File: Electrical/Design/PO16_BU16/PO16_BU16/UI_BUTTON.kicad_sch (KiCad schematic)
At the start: 32 parts

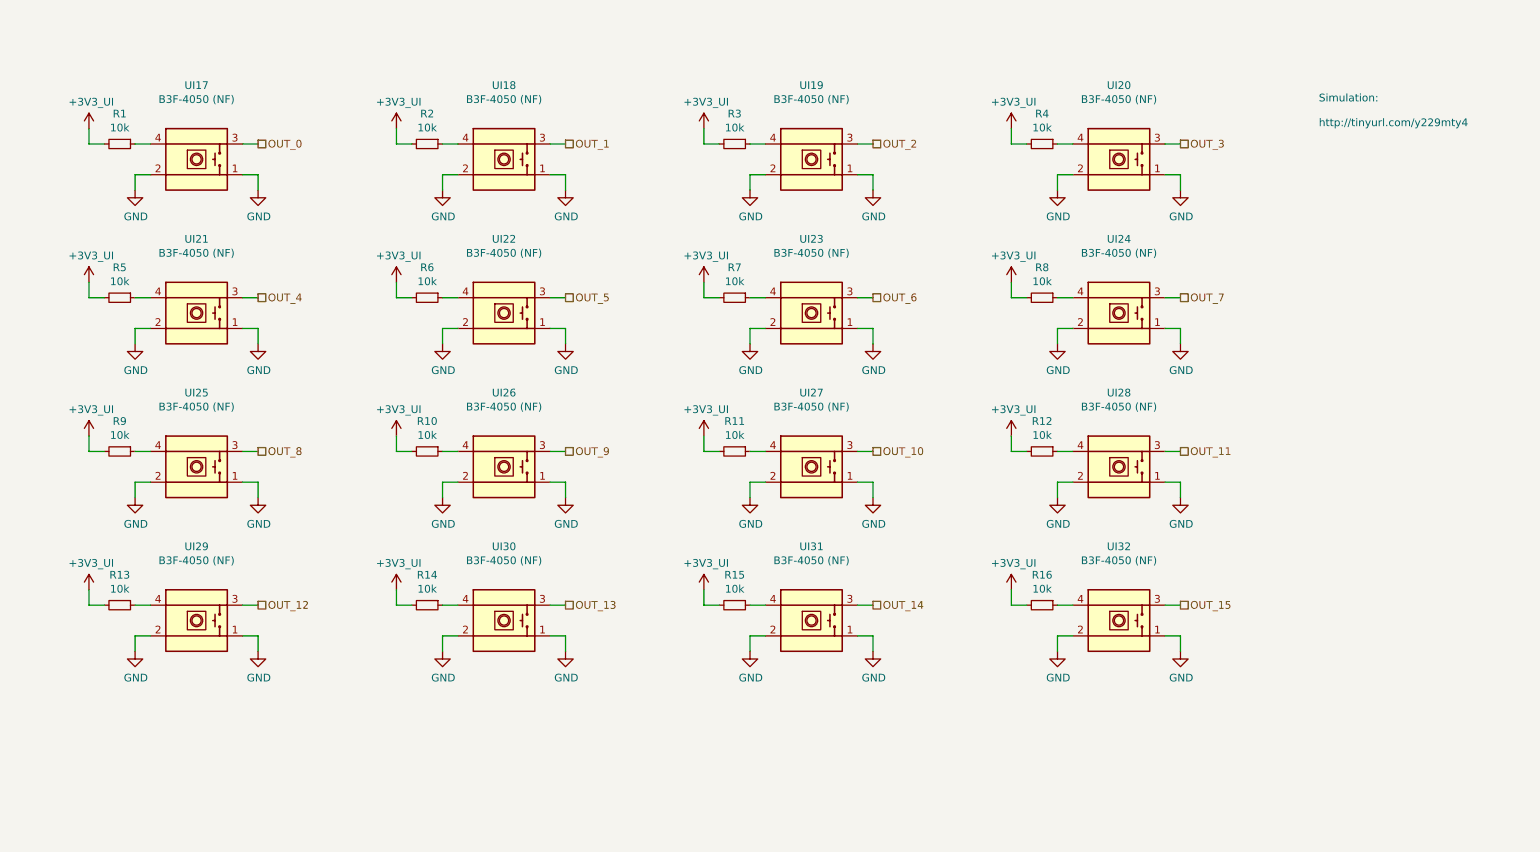
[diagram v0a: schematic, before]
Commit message: SUKU po16_bu16 cloned from pbf4
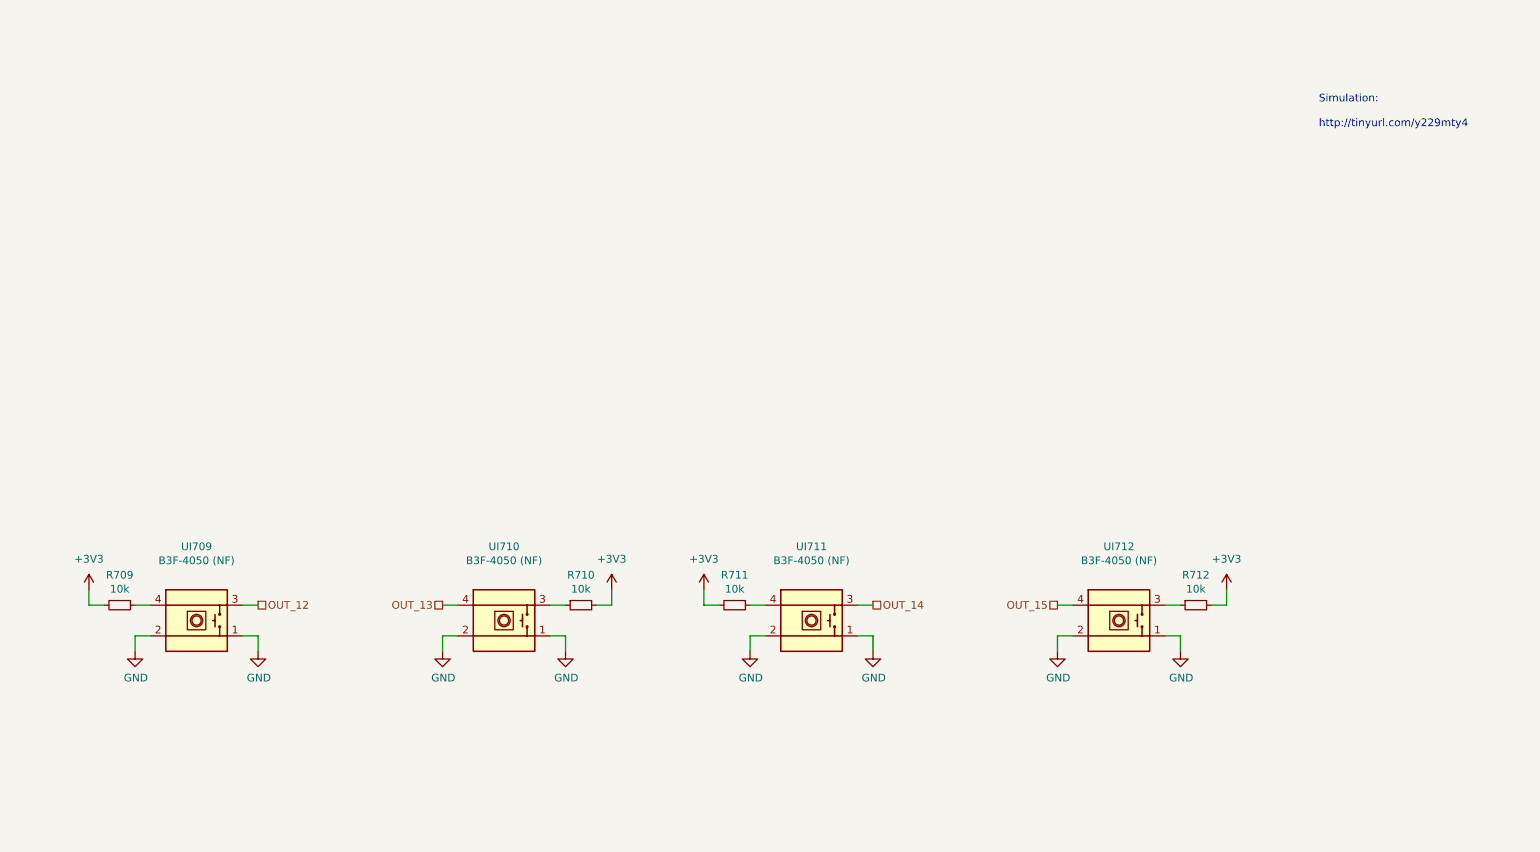
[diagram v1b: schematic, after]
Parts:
- removed R1, R10, R11, R12, R2, R3, R4, R5, R6, R7, R8, R9: 10k, suku_basics:RES_0805, symbol suku_basics:RES
- removed UI17, UI18, UI19, UI20, UI21, UI22, UI23, UI24, UI25, UI26, UI27, UI28: B3F-4050 (NF), suku_basics:UI_BUTTON_OMRON, symbol suku_basics:UI_Pushbutton_Omron
- R709: renamed from R13; footprint suku_basics:RES_0805 -> suku_basics:RES_0402
- R710: renamed from R14; footprint suku_basics:RES_0805 -> suku_basics:RES_0402
- R711: renamed from R15; footprint suku_basics:RES_0805 -> suku_basics:RES_0402
- R712: renamed from R16; footprint suku_basics:RES_0805 -> suku_basics:RES_0402
- renumbered UI29 to UI709, UI30 to UI710, UI31 to UI711, UI32 to UI712
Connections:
- net OUT_13: now also UI710.4; no longer UI710.3
- net OUT_15: now also UI712.4; no longer UI712.3
- net at R710.1: now also UI710.3; no longer UI710.4
- net at R712.1: now also UI712.3; no longer UI712.4
- net +3V3_UI renamed +3V3
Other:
- moved on the sheet: R710, R712

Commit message: SUKU PO16_BU16 updated design routed
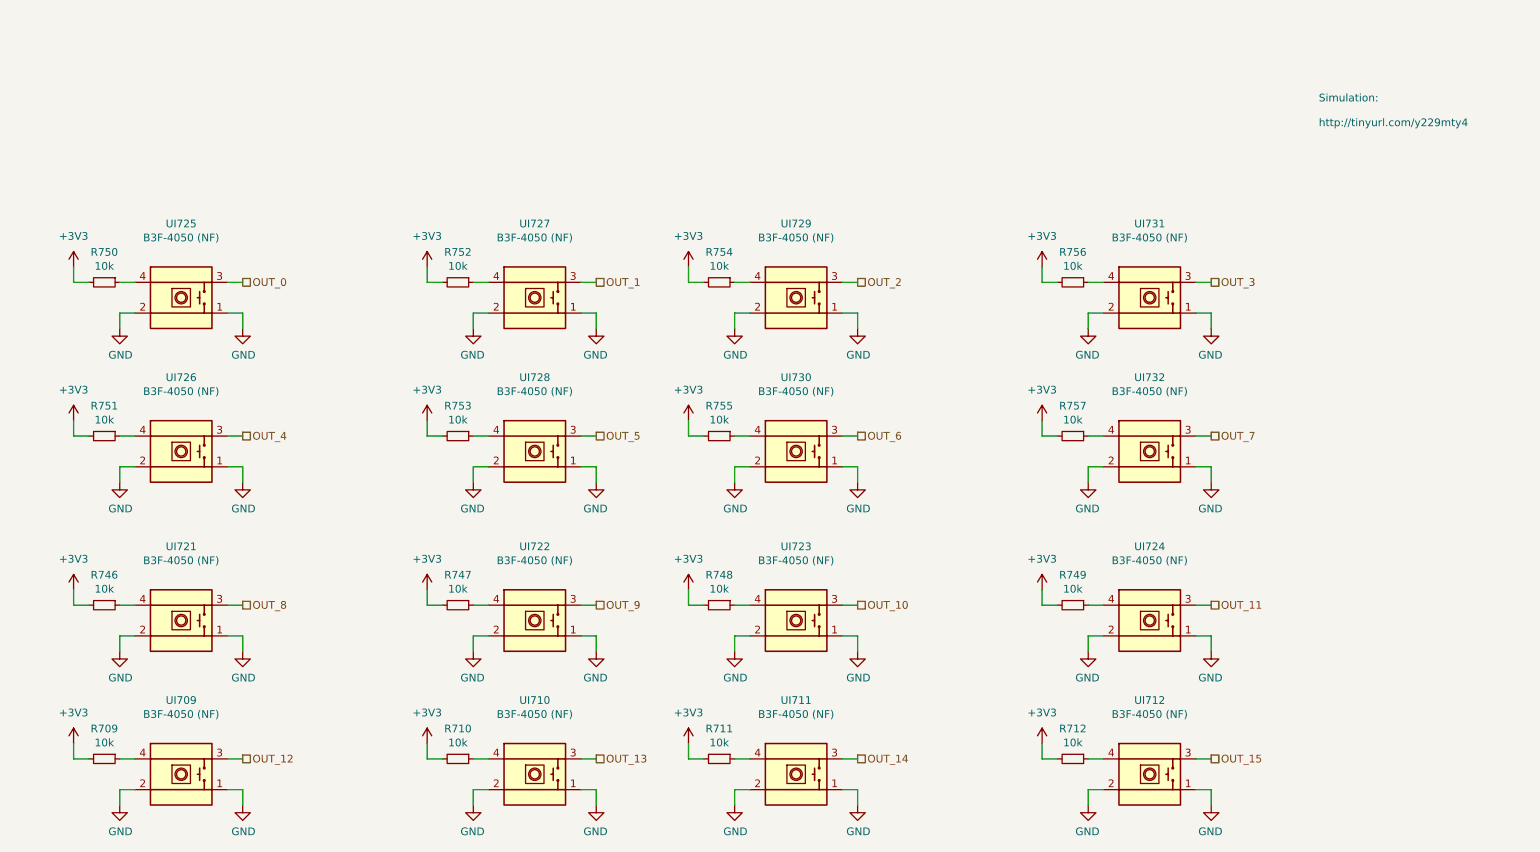
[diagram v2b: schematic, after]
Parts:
- added R746, R747, R748, R749, R750, R751, R752, R753, R754, R755, R756, R757: 10k, suku_basics:RES_0402, symbol suku_basics:RES
- added UI721, UI722, UI723, UI724, UI725, UI726, UI727, UI728, UI729, UI730, UI731, UI732: B3F-4050 (NF), suku_basics:UI_BUTTON_OMRON, symbol suku_basics:UI_Pushbutton_Omron
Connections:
- net +3V3: now also R746.2, R747.2, R748.2, R749.2, R750.2, R751.2, R752.2, R753.2, R754.2, R755.2, R756.2, R757.2
- net GND: now also UI721.1, UI721.2, UI722.1, UI722.2, UI723.1, UI723.2, UI724.1, UI724.2, UI725.1, UI725.2, UI726.1, UI726.2, UI727.1, UI727.2, UI728.1, UI728.2, UI729.1, UI729.2, UI730.1, UI730.2, UI731.1, UI731.2, UI732.1, UI732.2
- net OUT_13: now also UI710.3; no longer UI710.4
- net OUT_15: now also UI712.3; no longer UI712.4
- net at R710.1: now also UI710.4; no longer UI710.3
- net at R712.1: now also UI712.4; no longer UI712.3
- new net: R754.1, UI729.4
- new net: R753.1, UI728.4
- new net: R748.1, UI723.4
- new net: R747.1, UI722.4
- new net: R752.1, UI727.4
- new net: R746.1, UI721.4
- new net: R757.1, UI732.4
- new net: R756.1, UI731.4
- new net: R749.1, UI724.4
- new net: R750.1, UI725.4
- new net: R755.1, UI730.4
- new net: R751.1, UI726.4
- new net OUT_0: UI725.3
- new net OUT_1: UI727.3
- new net OUT_10: UI723.3
- new net OUT_11: UI724.3
- new net OUT_2: UI729.3
- new net OUT_3: UI731.3
- new net OUT_4: UI726.3
- new net OUT_5: UI728.3
- new net OUT_6: UI730.3
- new net OUT_7: UI732.3
- new net OUT_8: UI721.3
- new net OUT_9: UI722.3
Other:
- moved on the sheet: R709, R710, R711, R712, UI709, UI710, UI711, UI712

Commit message: SUKU PO16_BU16 sch reannotated
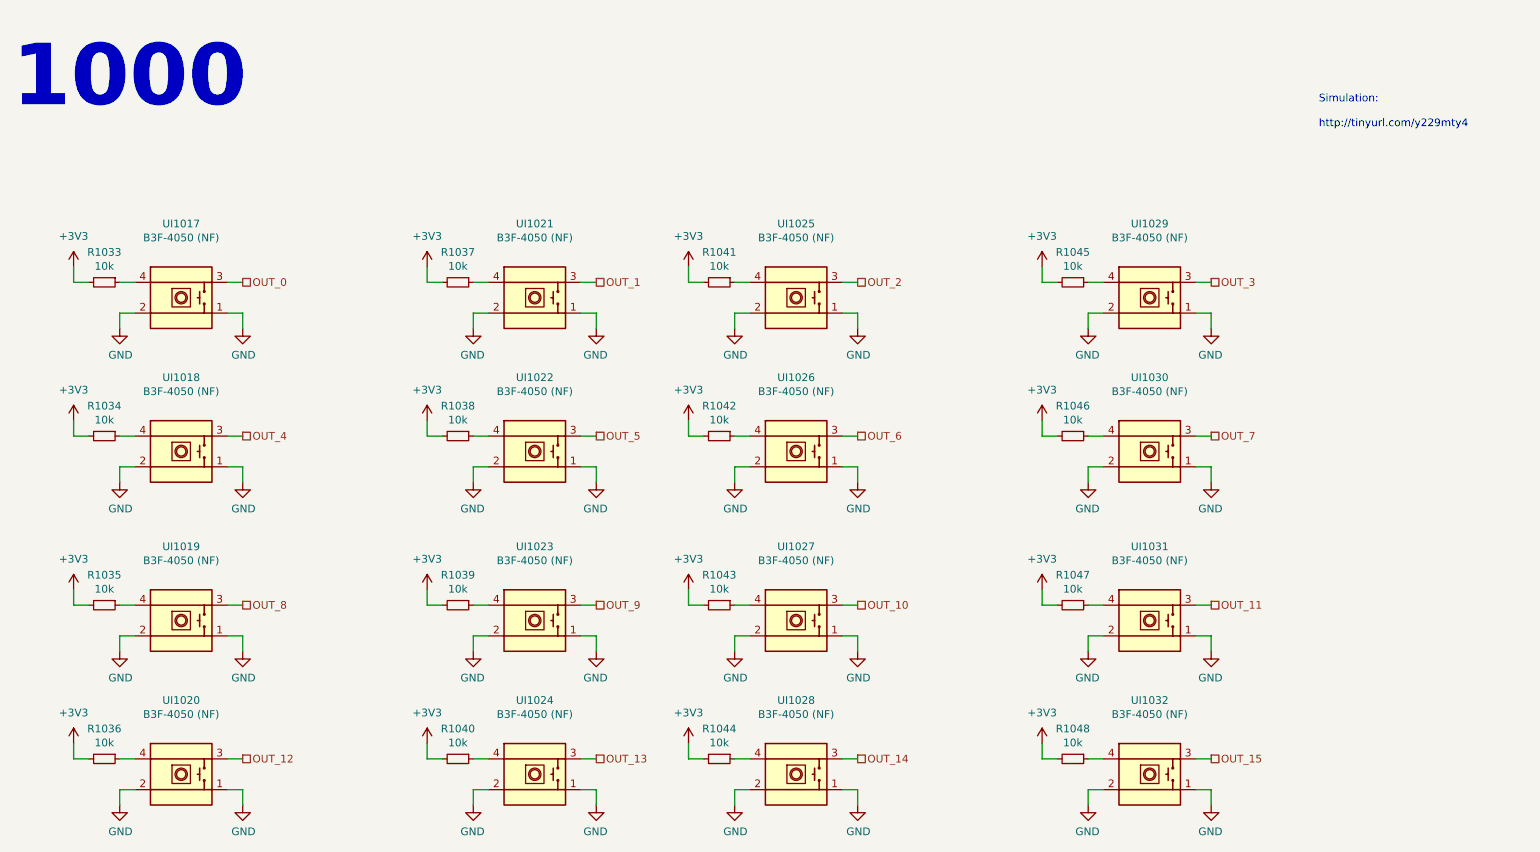
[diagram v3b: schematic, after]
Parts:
- renumbered R750 to R1033, R751 to R1034, R746 to R1035, R709 to R1036, R752 to R1037, R753 to R1038, R747 to R1039, R710 to R1040, R754 to R1041, R755 to R1042, R748 to R1043, R711 to R1044, R756 to R1045, R757 to R1046, R749 to R1047, R712 to R1048, UI725 to UI1017, UI726 to UI1018, UI721 to UI1019, UI709 to UI1020, UI727 to UI1021, UI728 to UI1022, UI722 to UI1023, UI710 to UI1024, UI729 to UI1025, UI730 to UI1026, UI723 to UI1027, UI711 to UI1028, UI731 to UI1029, UI732 to UI1030, UI724 to UI1031, UI712 to UI1032
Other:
- note added: "1000"

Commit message: SUKU via sizes and polygons updated
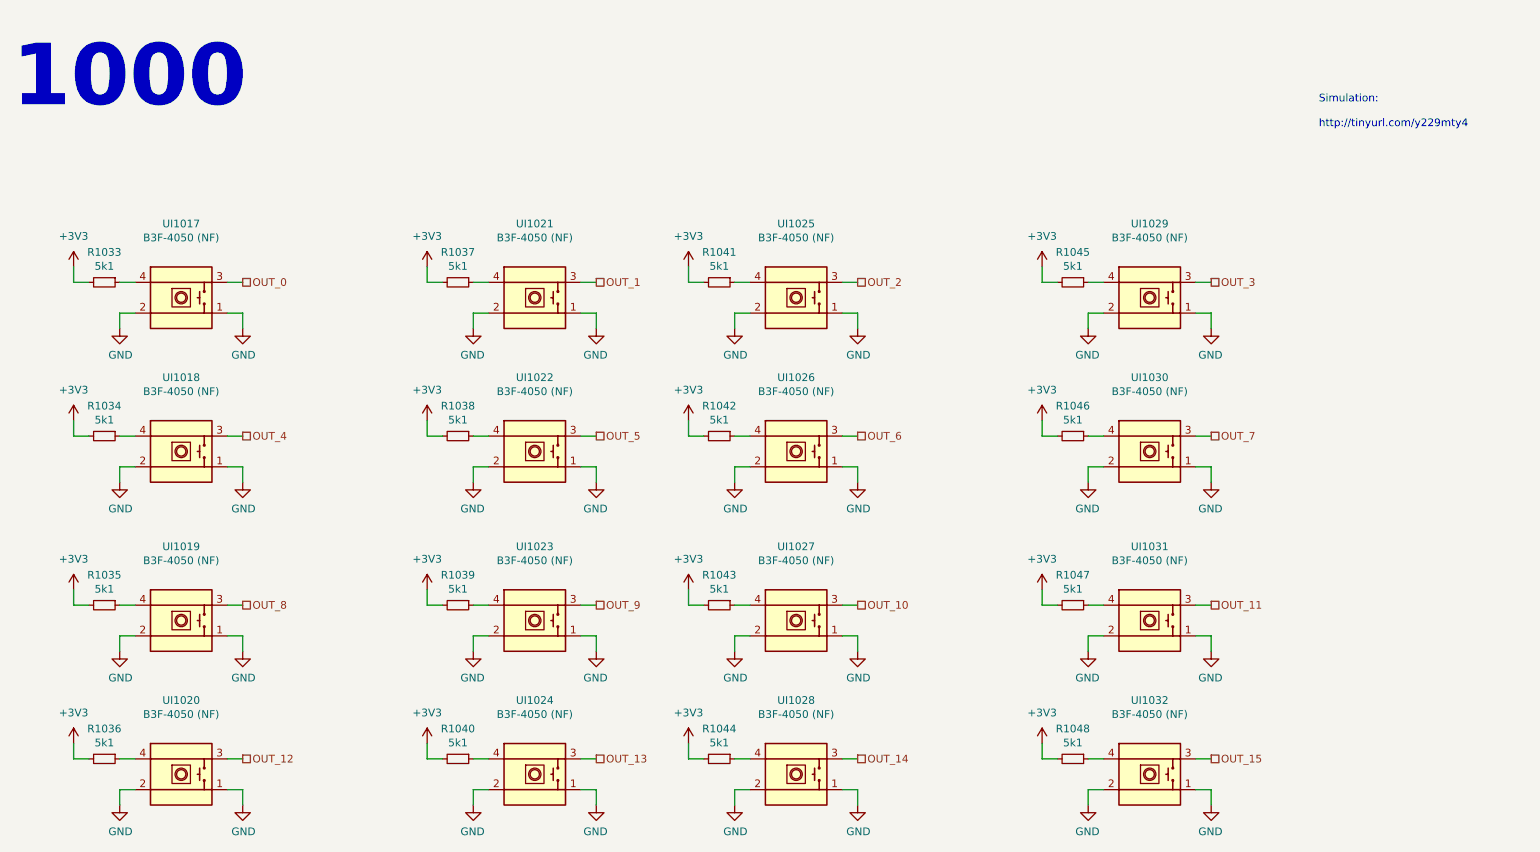
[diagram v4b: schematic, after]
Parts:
- R1033, R1034, R1035, R1036, R1037, R1038, R1039, R1040, R1041, R1042, R1043, R1044, R1045, R1046, R1047, R1048: value 10k -> 5k1
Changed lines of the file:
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@@
       (effects (font (size 1.27 1.27)))
     )
-    (property "Value" "10k" (at 35.56 134.493 90)
+    (property "Value" "5k1" (at 35.56 134.493 90)
       (effects (font (size 1.27 1.27)))
     )
@@
       (effects (font (size 1.27 1.27)))
     )
-    (property "Value" "10k" (at 93.98 134.493 90)
+    (property "Value" "5k1" (at 93.98 134.493 90)
       (effects (font (size 1.27 1.27)))
     )
@@
       (effects (font (size 1.27 1.27)))
     )
-    (property "Value" "10k" (at 137.16 134.493 90)
+    (property "Value" "5k1" (at 137.16 134.493 90)
       (effects (font (size 1.27 1.27)))
     )
@@
       (effects (font (size 1.27 1.27)))
     )
-    (property "Value" "10k" (at 195.58 134.493 90)
+    (property "Value" "5k1" (at 195.58 134.493 90)
       (effects (font (size 1.27 1.27)))
     )
@@
       (effects (font (size 1.27 1.27)))
     )
-    (property "Value" "10k" (at 137.16 55.753 90)
+    (property "Value" "5k1" (at 137.16 55.753 90)
       (effects (font (size 1.27 1.27)))
     )
@@
       (effects (font (size 1.27 1.27)))
     )
-    (property "Value" "10k" (at 93.98 55.753 90)
+    (property "Value" "5k1" (at 93.98 55.753 90)
       (effects (font (size 1.27 1.27)))
     )
@@
       (effects (font (size 1.27 1.27)))
     )
-    (property "Value" "10k" (at 195.58 81.153 90)
+    (property "Value" "5k1" (at 195.58 81.153 90)
       (effects (font (size 1.27 1.27)))
     )
@@
       (effects (font (size 1.27 1.27)))
     )
-    (property "Value" "10k" (at 195.58 55.753 90)
+    (property "Value" "5k1" (at 195.58 55.753 90)
       (effects (font (size 1.27 1.27)))
     )
@@
       (effects (font (size 1.27 1.27)))
     )
-    (property "Value" "10k" (at 195.58 109.093 90)
+    (property "Value" "5k1" (at 195.58 109.093 90)
       (effects (font (size 1.27 1.27)))
     )
@@
       (effects (font (size 1.27 1.27)))
     )
-    (property "Value" "10k" (at 93.98 109.093 90)
+    (property "Value" "5k1" (at 93.98 109.093 90)
       (effects (font (size 1.27 1.27)))
     )
@@
       (effects (font (size 1.27 1.27)))
     )
-    (property "Value" "10k" (at 93.98 81.153 90)
+    (property "Value" "5k1" (at 93.98 81.153 90)
       (effects (font (size 1.27 1.27)))
     )
@@
       (effects (font (size 1.27 1.27)))
     )
-    (property "Value" "10k" (at 137.16 109.093 90)
+    (property "Value" "5k1" (at 137.16 109.093 90)
       (effects (font (size 1.27 1.27)))
     )
@@
       (effects (font (size 1.27 1.27)))
     )
-    (property "Value" "10k" (at 35.56 109.093 90)
+    (property "Value" "5k1" (at 35.56 109.093 90)
       (effects (font (size 1.27 1.27)))
     )
@@
       (effects (font (size 1.27 1.27)))
     )
-    (property "Value" "10k" (at 35.56 81.153 90)
+    (property "Value" "5k1" (at 35.56 81.153 90)
       (effects (font (size 1.27 1.27)))
     )
@@
       (effects (font (size 1.27 1.27)))
     )
-    (property "Value" "10k" (at 35.56 55.753 90)
+    (property "Value" "5k1" (at 35.56 55.753 90)
       (effects (font (size 1.27 1.27)))
     )
@@
       (effects (font (size 1.27 1.27)))
     )
-    (property "Value" "10k" (at 137.16 81.153 90)
-      (effects (font (size 1.27 1.27)))
-    )
+    (property "Value" "5k1" (at 137.16 81.153 90)
+      (effects (font (size 1.27 1.27)))
+    )
